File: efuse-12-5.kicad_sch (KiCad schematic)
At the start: 13 parts, among them U9 TPS259472A

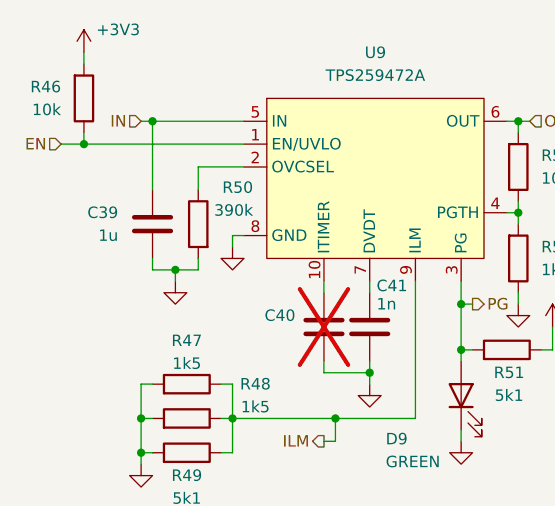
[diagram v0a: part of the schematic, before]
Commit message: schem: add disable jumper to efuses
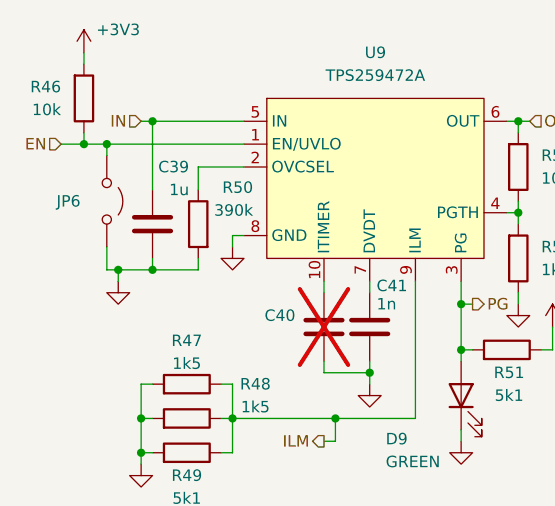
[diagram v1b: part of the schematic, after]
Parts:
- added JP6: Jumper_2_Small_Open, Connector_PinHeader_2.54mm:PinHeader_2x01_P2.54mm_Vertical, symbol Jumper:Jumper_2_Open
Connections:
- net EN: now also JP6.1 (A)
- net GND: now also JP6.2 (B)
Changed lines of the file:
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@@
-	)
-	(junction
-		(at 121.92 102.87)
-		(diameter 0)
-		(color 0 0 0 0)
 	)
 	(junction
@@
 	)
 	(junction
+		(at 119.38 102.87)
+		(diameter 0)
+		(color 0 0 0 0)
+	)
+	(junction
 		(at 118.11 119.38)
 		(diameter 0)
@@
 	)
 	(junction
+		(at 114.3 88.9)
+		(diameter 0)
+		(color 0 0 0 0)
+	)
+	(junction
 		(at 128.27 119.38)
 		(diameter 0)
@@
 	)
 	(junction
+		(at 115.57 102.87)
+		(diameter 0)
+		(color 0 0 0 0)
+	)
+	(junction
 		(at 153.67 111.76)
 		(diameter 0)
@@
 	(wire
 		(pts
-			(xy 121.92 102.87) (xy 124.46 102.87)
-		)
-		(stroke
-			(width 0)
-			(type default)
-		)
-	)
-	(wire
-		(pts
 			(xy 128.27 119.38) (xy 139.7 119.38)
 		)
@@
 	(wire
 		(pts
-			(xy 119.38 102.87) (xy 121.92 102.87)
+			(xy 119.38 102.87) (xy 124.46 102.87)
 		)
 		(stroke
@@
 	(wire
 		(pts
+			(xy 114.3 100.33) (xy 114.3 102.87)
+		)
+		(stroke
+			(width 0)
+			(type default)
+		)
+	)
+	(wire
+		(pts
+			(xy 114.3 102.87) (xy 115.57 102.87)
+		)
+		(stroke
+			(width 0)
+			(type default)
+		)
+	)
+	(wire
+		(pts
 			(xy 138.43 114.3) (xy 138.43 113.03)
 		)
@@
 	(wire
 		(pts
+			(xy 114.3 90.17) (xy 114.3 88.9)
+		)
+		(stroke
+			(width 0)
+			(type default)
+		)
+	)
+	(wire
+		(pts
 			(xy 160.02 105.41) (xy 160.02 106.68)
 		)
@@
 	(wire
 		(pts
+			(xy 114.3 88.9) (xy 129.54 88.9)
+		)
+		(stroke
+			(width 0)
+			(type default)
+		)
+	)
+	(wire
+		(pts
 			(xy 143.51 114.3) (xy 143.51 113.03)
 		)
@@
 	(wire
 		(pts
-			(xy 111.76 88.9) (xy 129.54 88.9)
+			(xy 111.76 88.9) (xy 114.3 88.9)
 		)
 		(stroke
@@
 	(wire
 		(pts
+			(xy 115.57 102.87) (xy 119.38 102.87)
+		)
+		(stroke
+			(width 0)
+			(type default)
+		)
+	)
+	(wire
+		(pts
 			(xy 160.02 96.52) (xy 160.02 95.25)
 		)
@@
 	(wire
 		(pts
-			(xy 121.92 102.87) (xy 121.92 104.14)
+			(xy 115.57 102.87) (xy 115.57 104.14)
 		)
 		(stroke
@@
 		(on_board yes)
 		(dnp no)
-		(fields_autoplaced yes)
 		(property "Reference" "C39"
-			(at 115.57 96.5199 0)
+			(at 123.444 91.44 0)
 			(effects
 				(font
@@
 		)
 		(property "Value" "1u"
-			(at 115.57 99.0599 0)
+			(at 123.444 93.98 0)
 			(effects
 				(font
@@
 	)
 	(symbol
+		(lib_id "Jumper:Jumper_2_Open")
+		(at 114.3 95.25 270)
+		(unit 1)
+		(exclude_from_sim no)
+		(in_bom yes)
+		(on_board yes)
+		(dnp no)
+		(property "Reference" "JP6"
+			(at 108.712 95.25 90)
+			(effects
+				(font
+					(size 1.27 1.27)
+				)
+				(justify left)
+			)
+		)
+		(property "Value" "Jumper_2_Small_Open"
+			(at 118.11 95.25 0)
+			(effects
+				(font
+					(size 1.27 1.27)
+				)
+				(hide yes)
+			)
+		)
+		(property "Footprint" "Connector_PinHeader_2.54mm:PinHeader_2x01_P2.54mm_Vertical"
+			(at 114.3 95.25 0)
+			(effects
+				(font
+					(size 1.27 1.27)
+				)
+				(hide yes)
+			)
+		)
+		(property "Datasheet" "~"
+			(at 114.3 95.25 0)
+			(effects
+				(font
+					(size 1.27 1.27)
+				)
+				(hide yes)
+			)
+		)
+		(property "Description" "Jumper, 2-pole, open"
+			(at 114.3 95.25 0)
+			(effects
+				(font
+					(size 1.27 1.27)
+				)
+				(hide yes)
+			)
+		)
+		(pin "2"
+		)
+		(pin "1"
+		)
+		(instances
+			(project "valrob-carte-alim-cdf-1"
+				(path "/8d7b287d-627f-46aa-8c27-0b5ed29ab4a2/007b07d4-119b-4744-aa24-fabc828b541b/2da8bdbe-fbad-48e0-8074-270f50ca7ae9"
+					(reference "JP9")
+					(unit 1)
+				)
+				(path "/8d7b287d-627f-46aa-8c27-0b5ed29ab4a2/007b07d4-119b-4744-aa24-fabc828b541b/897efccf-9ba0-4cd0-920a-43d7da1c794b"
+					(reference "JP7")
+					(unit 1)
+				)
+				(path "/8d7b287d-627f-46aa-8c27-0b5ed29ab4a2/007b07d4-119b-4744-aa24-fabc828b541b/a7541f7c-679e-41f8-9efa-18ff84fb26c0"
+					(reference "JP6")
+					(unit 1)
+				)
+				(path "/8d7b287d-627f-46aa-8c27-0b5ed29ab4a2/007b07d4-119b-4744-aa24-fabc828b541b/c68fcf24-d266-4575-8fd9-b617598010ac"
+					(reference "JP8")
+					(unit 1)
+				)
+			)
+		)
+	)
+	(symbol
 		(lib_id "GLCS:TPS259472x")
 		(at 144.78 91.44 0)
@@
 	(symbol
 		(lib_id "power:GND")
-		(at 121.92 104.14 0)
+		(at 115.57 104.14 0)
 		(unit 1)
 		(exclude_from_sim no)
@@
 		(fields_autoplaced yes)
 		(property "Reference" "#PWR087"
-			(at 121.92 110.49 0)
+			(at 115.57 110.49 0)
 			(effects
 				(font
@@
 		)
 		(property "Value" "GND"
-			(at 121.92 109.22 0)
+			(at 115.57 109.22 0)
 			(effects
 				(font
@@
 		)
 		(property "Footprint" ""
-			(at 121.92 104.14 0)
+			(at 115.57 104.14 0)
 			(effects
 				(font
@@
 		)
 		(property "Datasheet" ""
-			(at 121.92 104.14 0)
+			(at 115.57 104.14 0)
 			(effects
 				(font
@@
 		)
 		(property "Description" "Power symbol creates a global label with name \"GND\" , ground"
-			(at 121.92 104.14 0)
-			(effects
-				(font
+			(at 115.57 104.14 0)
+			(effects
+				(font

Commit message: schem: update TPS259472A symbol
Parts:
- U9: footprint (none) -> GLCS:Texas_RPW0010A_VQFN-HR-10_2x2mm_P0.5mm
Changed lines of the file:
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@@
 			)
 		)
-		(property "Footprint" ""
+		(property "Footprint" "GLCS:Texas_RPW0010A_VQFN-HR-10_2x2mm_P0.5mm"
 			(at 144.78 91.44 0)
 			(effects

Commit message: schem: add sheet title
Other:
- company: (none) -> Valrobotik
- title: (none) -> Carte alim CDF 1
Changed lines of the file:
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@@
 	(generator_version "9.0")
 	(paper "A4")
+	(title_block
+		(title "Carte alim CDF 1")
+		(date "2026-01-15")
+		(rev "01")
+		(company "Valrobotik")
+	)
 	(text "Slew Rate\n2A limit for 500uF load\n-> 4V/ms\n-> Cdvdt = 500pF\n(BOM consolidation) For 1n -> SR = 2V/ms\n\nIlim\nReq=653.85Ω\n->Ilim=5.1A\n->I=Vilm(µV)/(180*650)"
 		(exclude_from_sim no)

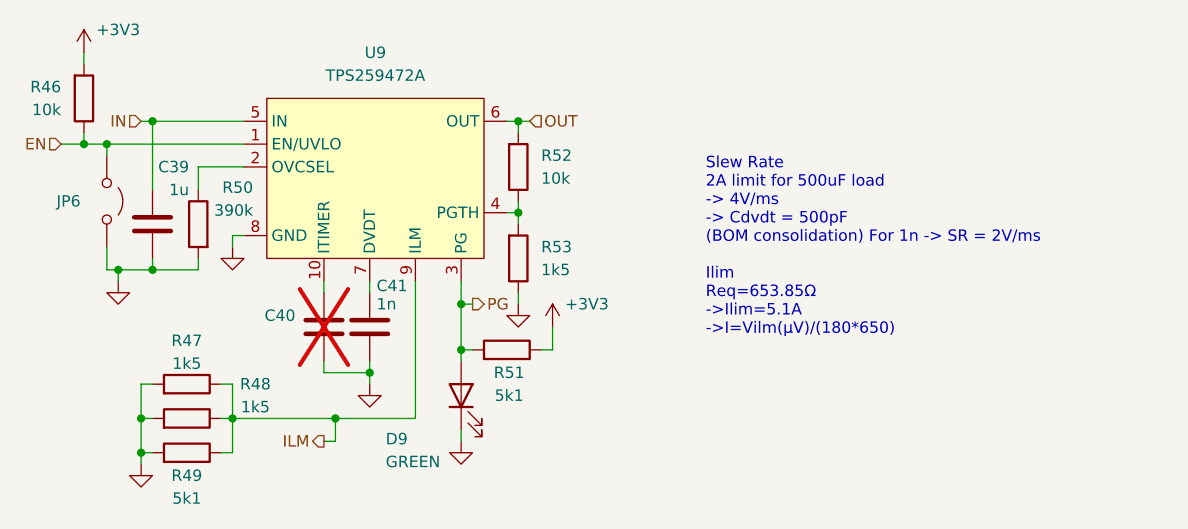
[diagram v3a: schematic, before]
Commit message: schem: renumber
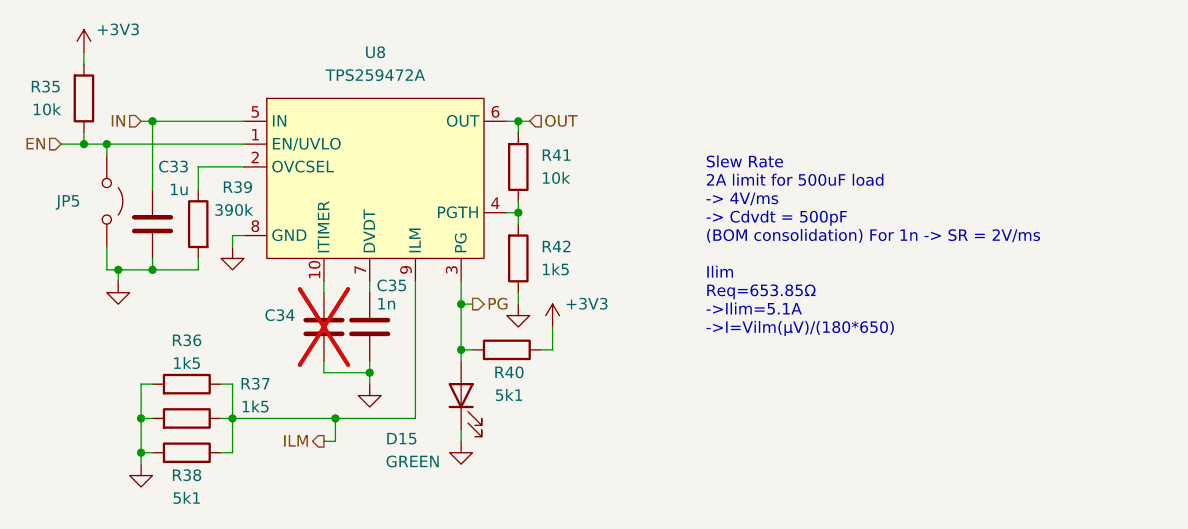
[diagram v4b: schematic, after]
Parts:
- renumbered C39 to C33, C40 to C34, C41 to C35, D9 to D15, JP6 to JP5, R46 to R35, R47 to R36, R48 to R37, R49 to R38, R50 to R39, R51 to R40, R52 to R41, R53 to R42, U9 to U8
